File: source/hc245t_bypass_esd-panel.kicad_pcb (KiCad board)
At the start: 2 copper layers, 48 x 48 mm, 180 parts, among them J1 74HC245, U1 NUP4202, U2 NUP4202

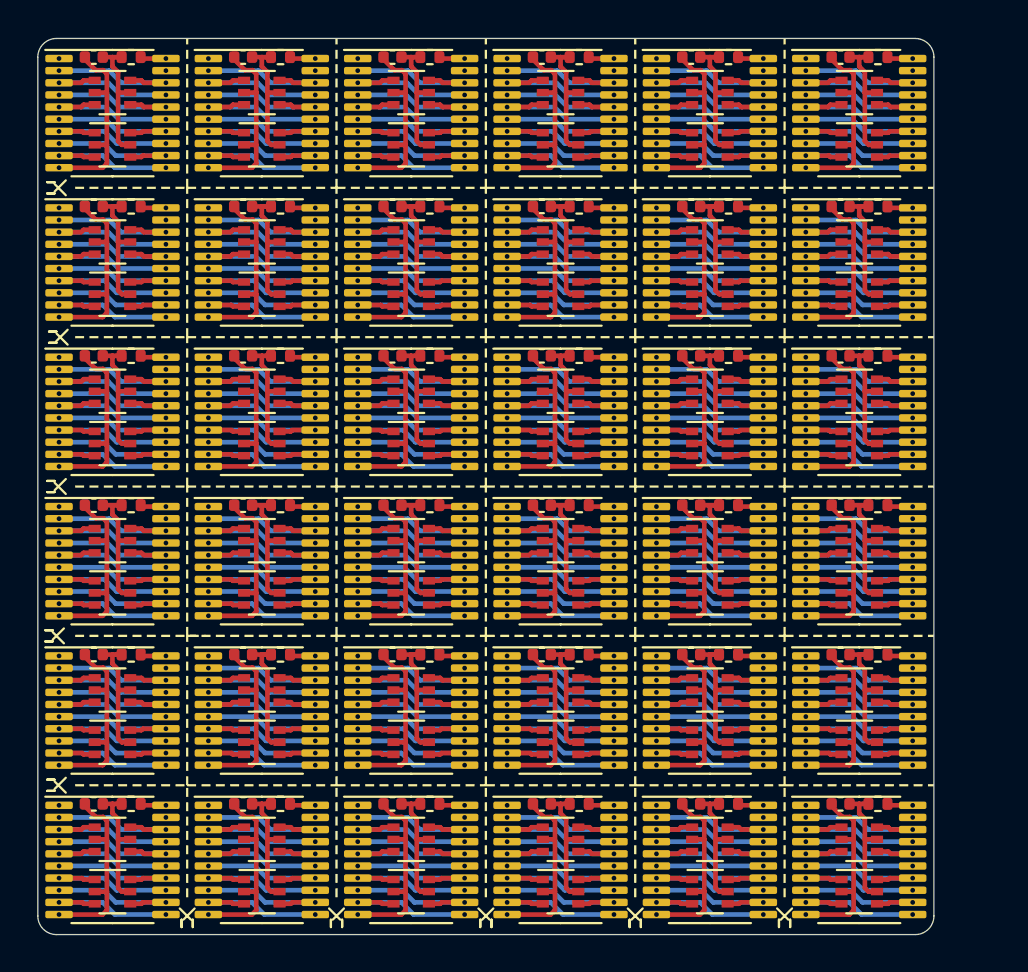
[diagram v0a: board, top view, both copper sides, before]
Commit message: made pannel 5x3 instead of 6x6
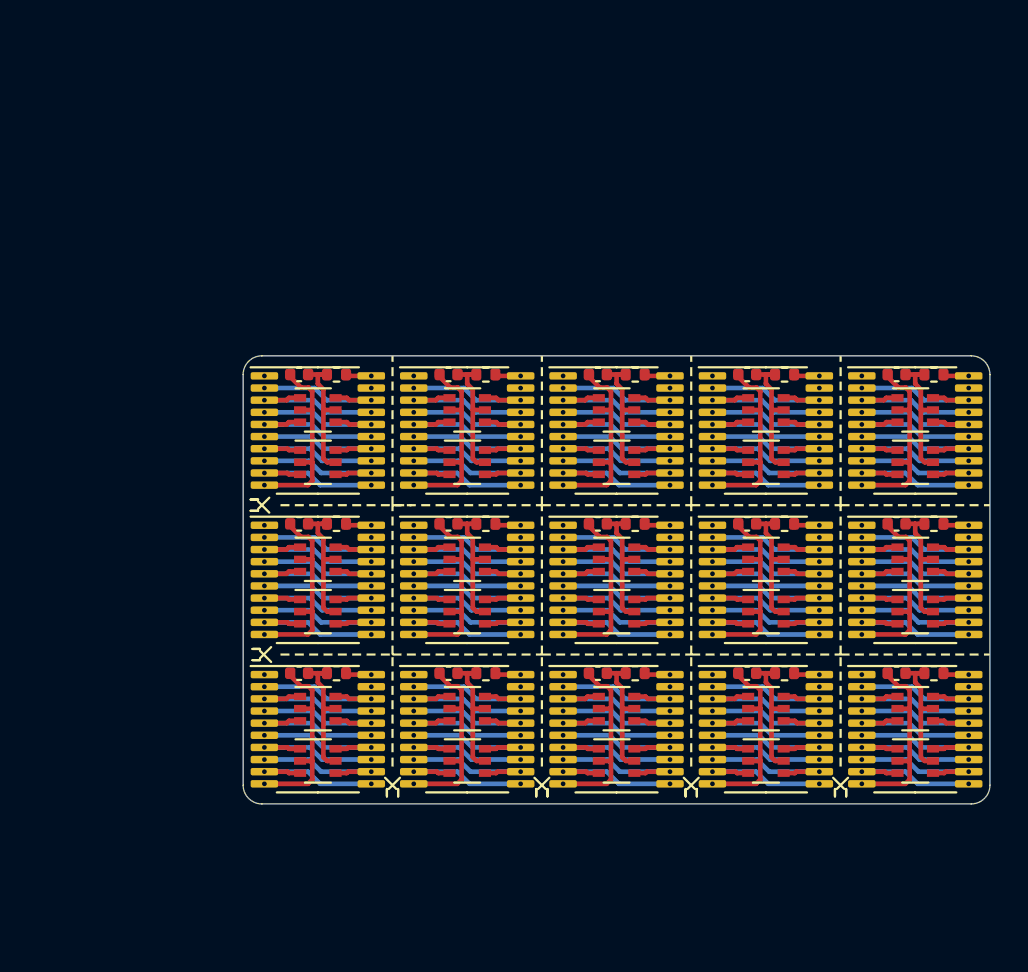
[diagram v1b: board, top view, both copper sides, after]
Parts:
- removed the C1 at (159.0, 127.0)
- removed the C1 at (159.0, 103.0)
- removed the C1 at (159.0, 119.0)
- removed the C1 at (127.0, 103.0)
- removed the C1 at (127.0, 95.0)
- removed the C1 at (159.0, 111.0)
- removed the C1 at (119.0, 87.0)
- removed the C1 at (159.0, 95.0)
- removed the C1 at (135.0, 95.0)
- removed the C1 at (119.0, 103.0)
- removed the C1 at (151.0, 95.0)
- removed the C1 at (159.0, 87.0)
- removed the C1 at (119.0, 95.0)
- removed the C1 at (143.0, 87.0)
- removed the C1 at (127.0, 87.0)
- removed the C1 at (151.0, 103.0)
- removed the C1 at (135.0, 87.0)
- removed the C1 at (143.0, 103.0)
- removed the C1 at (135.0, 103.0)
- removed the C1 at (151.0, 87.0)
- removed the C1 at (143.0, 95.0)
- removed the J1 at (160.0, 98.0)
- removed the J1 at (120.0, 90.0)
- removed the J1 at (120.0, 106.0)
- removed the J1 at (152.0, 98.0)
- removed the J1 at (144.0, 106.0)
- removed the J1 at (160.0, 114.0)
- removed the J1 at (128.0, 98.0)
- removed the J1 at (160.0, 90.0)
- removed the J1 at (144.0, 98.0)
- removed the J1 at (136.0, 106.0)
- removed the J1 at (160.0, 122.0)
- removed the J1 at (152.0, 90.0)
- removed the J1 at (144.0, 90.0)
- removed the J1 at (120.0, 98.0)
- removed the J1 at (136.0, 98.0)
- removed the J1 at (160.0, 106.0)
- removed the J1 at (152.0, 106.0)
- removed the J1 at (128.0, 106.0)
- removed the J1 at (160.0, 130.0)
- removed the J1 at (128.0, 90.0)
- removed the J1 at (136.0, 90.0)
- removed the R1 at (137.0, 95.0)
- removed the R1 at (129.0, 87.0)
- removed the R1 at (153.0, 95.0)
- removed the R1 at (137.0, 103.0)
- removed the R1 at (145.0, 87.0)
- removed the R1 at (121.0, 103.0)
- removed the R1 at (145.0, 103.0)
- removed the R1 at (129.0, 95.0)
- removed the R1 at (161.0, 87.0)
- removed the R1 at (153.0, 103.0)
- removed the R1 at (153.0, 87.0)
- removed the R1 at (121.0, 87.0)
- removed the R1 at (121.0, 95.0)
- removed the R1 at (145.0, 95.0)
- removed the R1 at (161.0, 95.0)
- removed the R1 at (161.0, 103.0)
- removed the R1 at (137.0, 87.0)
- removed the R1 at (161.0, 111.0)
- removed the R1 at (129.0, 103.0)
- removed the R1 at (161.0, 119.0)
- removed the R1 at (161.0, 127.0)
- removed the U1 at (160.0, 88.9)
- removed the U1 at (120.0, 88.9)
- removed the U1 at (136.0, 88.9)
- removed the U1 at (120.0, 104.9)
- removed the U1 at (160.0, 96.9)
- removed the U1 at (128.0, 96.9)
- removed the U1 at (152.0, 104.9)
- removed the U1 at (136.0, 96.9)
- removed the U1 at (120.0, 96.9)
- removed the U1 at (136.0, 104.9)
- removed the U1 at (144.0, 104.9)
- removed the U1 at (160.0, 128.9)
- removed the U1 at (144.0, 96.9)
- removed the U1 at (160.0, 104.9)
- removed the U1 at (152.0, 88.9)
- removed the U1 at (144.0, 88.9)
- removed the U1 at (152.0, 96.9)
- removed the U1 at (160.0, 112.9)
- removed the U1 at (128.0, 104.9)
- removed the U1 at (128.0, 88.9)
- removed the U1 at (160.0, 120.9)
- removed the U2 at (120.0, 91.7)
- removed the U2 at (152.0, 107.7)
- removed the U2 at (144.0, 107.7)
- removed the U2 at (128.0, 107.7)
- removed the U2 at (136.0, 99.7)
- removed the U2 at (160.0, 99.7)
- removed the U2 at (160.0, 107.7)
- removed the U2 at (120.0, 99.7)
- removed the U2 at (160.0, 131.7)
- removed the U2 at (152.0, 99.7)
- removed the U2 at (128.0, 99.7)
- removed the U2 at (136.0, 91.7)
- removed the U2 at (160.0, 91.7)
- removed the U2 at (160.0, 123.7)
- removed the U2 at (120.0, 107.7)
- removed the U2 at (144.0, 91.7)
- removed the U2 at (136.0, 107.7)
- removed the U2 at (128.0, 91.7)
- removed the U2 at (152.0, 91.7)
- removed the U2 at (144.0, 99.7)
- removed the U2 at (160.0, 115.7)
- moved C1 13.0 mm to (138.0, 104.0)
- moved C1 13.0 mm to (146.0, 104.0)
- moved C1 13.0 mm to (154.0, 104.0)
- moved C1 13.0 mm to (154.0, 120.0)
- moved C1 13.0 mm to (130.0, 120.0)
- moved C1 13.0 mm to (162.0, 104.0)
- moved C1 13.0 mm to (162.0, 112.0)
- moved C1 13.0 mm to (138.0, 120.0)
- moved C1 13.0 mm to (138.0, 112.0)
- moved C1 13.0 mm to (162.0, 120.0)
- moved C1 13.0 mm to (146.0, 120.0)
- moved C1 13.0 mm to (146.0, 112.0)
- moved C1 13.0 mm to (154.0, 112.0)
- moved C1 13.0 mm to (130.0, 112.0)
- moved C1 13.0 mm to (130.0, 104.0)
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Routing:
- net (no net): track 2965.1 -> 1235.5 mm
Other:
- board size 48 x 48 mm -> 40 x 24 mm
